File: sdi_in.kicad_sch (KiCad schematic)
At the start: 20 parts, among them J1 Conn_Coaxial, U1 LMH0344SQE_NOPB

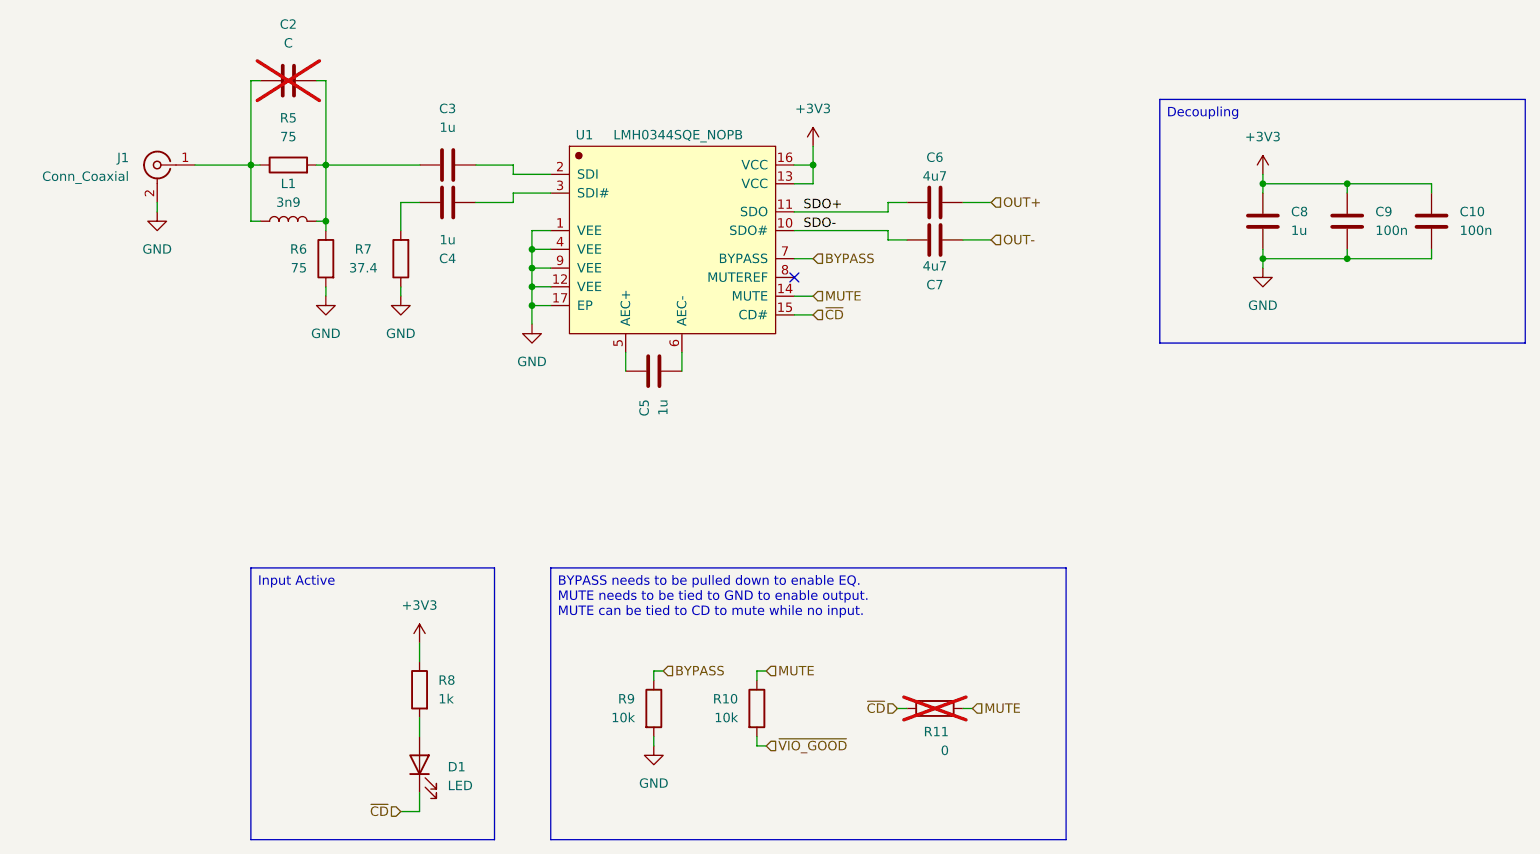
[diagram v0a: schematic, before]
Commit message: add power led and test points
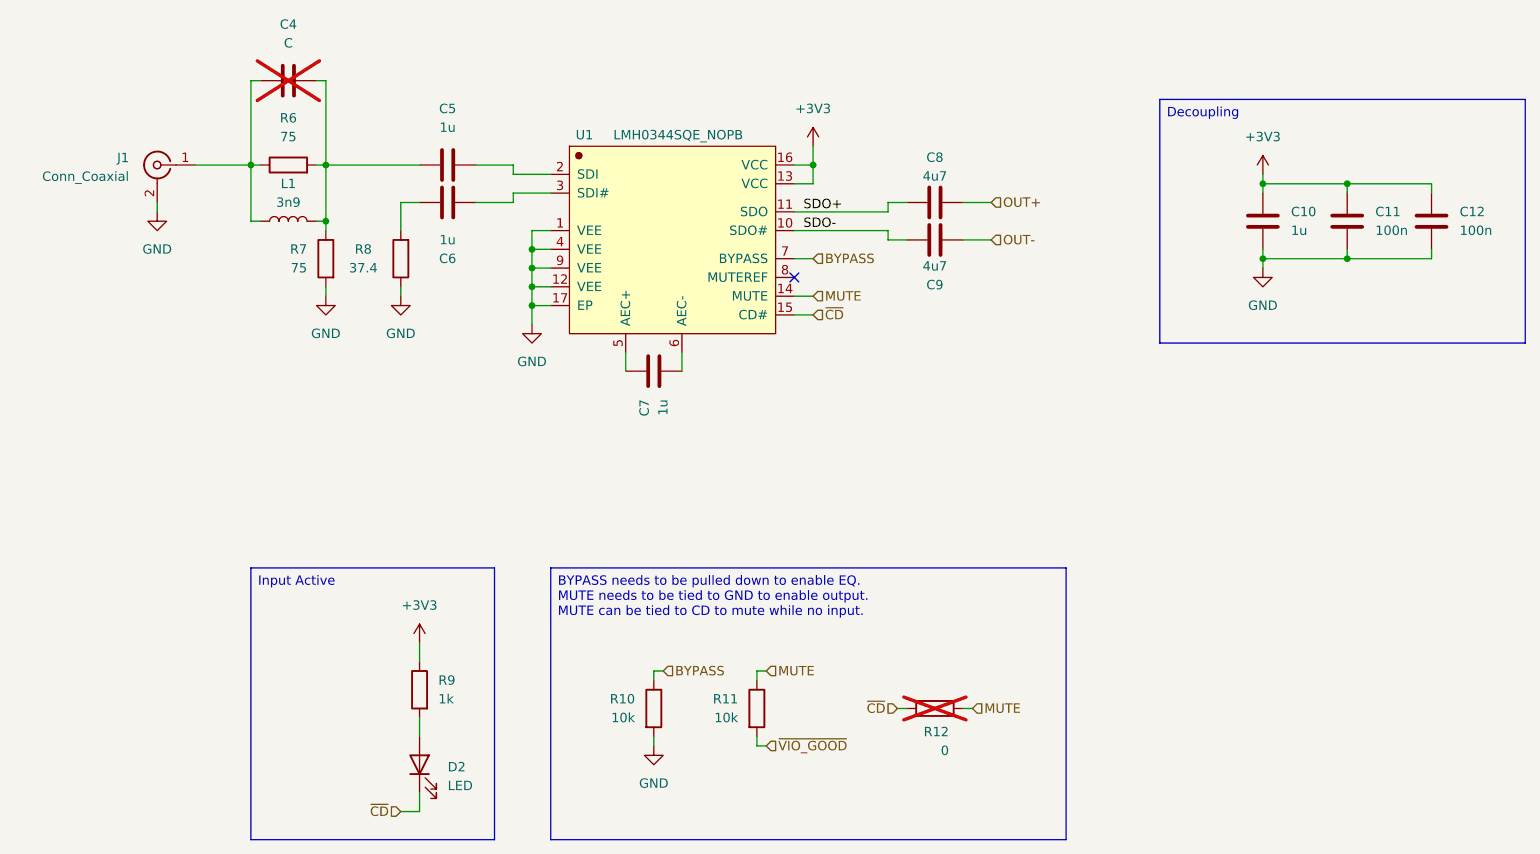
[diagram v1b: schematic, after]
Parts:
- renumbered C8 to C10, C9 to C11, C10 to C12, C2 to C4, C3 to C5, C4 to C6, C5 to C7, C6 to C8, C7 to C9, D1 to D2, R9 to R10, R10 to R11, R11 to R12, R5 to R6, R6 to R7, R7 to R8, R8 to R9

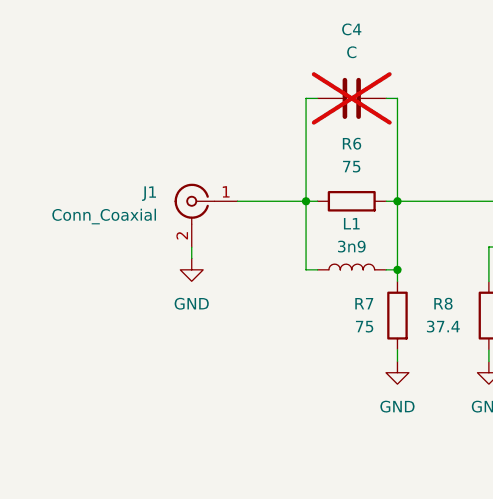
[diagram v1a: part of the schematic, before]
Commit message: check against jlcpcb capabilities
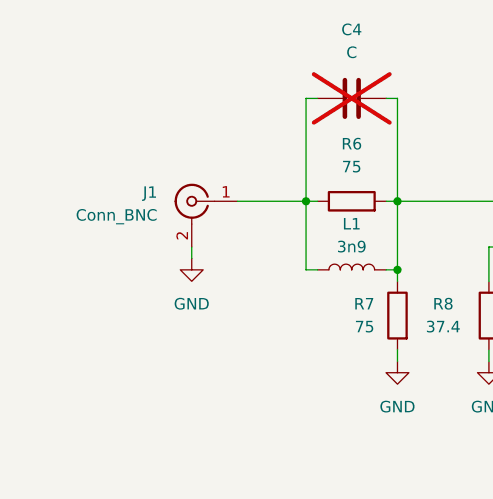
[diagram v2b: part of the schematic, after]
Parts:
- J1: value Conn_Coaxial -> Conn_BNC
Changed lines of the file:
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@@
 			)
 		)
-		(property "Value" "Conn_Coaxial"
+		(property "Value" "Conn_BNC"
 			(at 50.8 70.1431 0)
 			(show_name no)

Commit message: add some larger bypass caps to the cable drivers
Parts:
- renumbered C9 to C10, C10 to C11, C11 to C12, C12 to C13, C4 to C5, C5 to C6, C6 to C7, C7 to C8, C8 to C9

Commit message: specify skus for parts
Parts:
- C10, C9: LCSC (none) -> C69335
- C11, C8: LCSC (none) -> C6119818
- C12, C13: LCSC (none) -> C282519
- C6, C7: LCSC (none) -> C29266
- L1: LCSC (none) -> C412279
- R10, R11: LCSC (none) -> C25804
- R12: LCSC (none) -> C15402
- R6, R7: LCSC (none) -> C324774
- R8: LCSC (none) -> C2091522
- R9: LCSC (none) -> C21190
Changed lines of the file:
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@@
+			)
+		)
+		(property "LCSC" "C25804"
+			(at 121.92 142.24 0)
+			(hide yes)
+			(show_name no)
+			(do_not_autoplace no)
+			(effects
+				(font
+					(size 1.27 1.27)
+				)
 			)
 		)
@@
 			)
 		)
+		(property "LCSC" "C69335"
+			(at 160.02 73.66 90)
+			(hide yes)
+			(show_name no)
+			(do_not_autoplace no)
+			(effects
+				(font
+					(size 1.27 1.27)
+				)
+			)
+		)
 		(pin "2"
 		)
@@
 			)
 		)
+		(property "LCSC" "C29266"
+			(at 93.98 73.66 90)
+			(hide yes)
+			(show_name no)
+			(do_not_autoplace no)
+			(effects
+				(font
+					(size 1.27 1.27)
+				)
+			)
+		)
 		(pin "1"
 		)
@@
 		(property "KiLib_Generator" "SMD_2terminal_chip_molded"
 			(at 160.02 142.24 0)
+			(hide yes)
+			(show_name no)
+			(do_not_autoplace no)
+			(effects
+				(font
+					(size 1.27 1.27)
+				)
+			)
+		)
+		(property "LCSC" "C15402"
+			(at 160.02 142.24 90)
 			(hide yes)
 			(show_name no)
@@
 			)
 		)
+		(property "LCSC" "C412279"
+			(at 72.39 76.2 90)
+			(hide yes)
+			(show_name no)
+			(do_not_autoplace no)
+			(effects
+				(font
+					(size 1.27 1.27)
+				)
+			)
+		)
 		(pin "2"
 		)
@@
 			)
 		)
+		(property "LCSC" "C324774"
+			(at 72.39 68.58 90)
+			(hide yes)
+			(show_name no)
+			(do_not_autoplace no)
+			(effects
+				(font
+					(size 1.27 1.27)
+				)
+			)
+		)
 		(pin "2"
 		)
@@
 			)
 		)
+		(property "LCSC" "C69335"
+			(at 160.02 78.74 90)
+			(hide yes)
+			(show_name no)
+			(do_not_autoplace no)
+			(effects
+				(font
+					(size 1.27 1.27)
+				)
+			)
+		)
 		(pin "2"
 		)
@@
 		)
 		(property "KiLib_Generator" "SMD_2terminal_chip_molded"
+			(at 121.92 96.52 0)
+			(hide yes)
+			(show_name no)
+			(do_not_autoplace no)
+			(effects
+				(font
+					(size 1.27 1.27)
+				)
+			)
+		)
+		(property "LCSC" "C6119818"
 			(at 121.92 96.52 0)
 			(hide yes)
@@
 			)
 		)
+		(property "LCSC" "C29266"
+			(at 93.98 68.58 90)
+			(hide yes)
+			(show_name no)
+			(do_not_autoplace no)
+			(effects
+				(font
+					(size 1.27 1.27)
+				)
+			)
+		)
 		(pin "1"
 		)
@@
 		)
 		(property "KiLib_Generator" "SMD_2terminal_chip_molded"
+			(at 135.89 142.24 0)
+			(hide yes)
+			(show_name no)
+			(do_not_autoplace no)
+			(effects
+				(font
+					(size 1.27 1.27)
+				)
+			)
+		)
+		(property "LCSC" "C25804"
 			(at 135.89 142.24 0)
 			(hide yes)
@@
 			)
 		)
+		(property "LCSC" "C21190"
+			(at 90.17 139.7 0)
+			(hide yes)
+			(show_name no)
+			(do_not_autoplace no)
+			(effects
+				(font
+					(size 1.27 1.27)
+				)
+			)
+		)
 		(pin "1"
 		)
@@
 			)
 		)
+		(property "LCSC" "C6119818"
+			(at 204.47 76.2 0)
+			(hide yes)
+			(show_name no)
+			(do_not_autoplace no)
+			(effects
+				(font
+					(size 1.27 1.27)
+				)
+			)
+		)
 		(pin "2"
 		)
@@
 			)
 		)
+		(property "LCSC" "C282519"
+			(at 227.33 76.2 0)
+			(hide yes)
+			(show_name no)
+			(do_not_autoplace no)
+			(effects
+				(font
+					(size 1.27 1.27)
+				)
+			)
+		)
 		(pin "2"
 		)
@@
 			)
 		)
+		(property "LCSC" "C282519"
+			(at 215.9 76.2 0)
+			(hide yes)
+			(show_name no)
+			(do_not_autoplace no)
+			(effects
+				(font
+					(size 1.27 1.27)
+				)
+			)
+		)
 		(pin "2"
 		)
@@
 			)
 		)
+		(property "LCSC" "C2091522"
+			(at 87.63 81.28 0)
+			(hide yes)
+			(show_name no)
+			(do_not_autoplace no)
+			(effects
+				(font
+					(size 1.27 1.27)
+				)
+			)
+		)
 		(pin "2"
 		)
@@
 			(at 77.47 81.28 0)
 			(hide yes)
+			(show_name no)
+			(do_not_autoplace no)
+			(effects
+				(font
+					(size 1.27 1.27)
+				)
+			)
+		)
+		(property "LCSC" "C324774"
+			(at 77.47 81.28 0)
+			(hide yes)

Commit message: specify led colours
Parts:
- D2: value LED -> LED Green
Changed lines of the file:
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@@
 		(exclude_from_sim no)
 		(at 67.31 123.19 0)
-		(size 33.02 36.83)
+		(size 38.1 36.83)
 		(margins 0.9525 0.9525 0.9525 0.9525)
 		(stroke
@@
 			)
 		)
-		(property "Value" "LED"
+		(property "Value" "LED Green"
 			(at 93.98 152.7174 90)
 			(show_name no)

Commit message: sku and led resistor updates following review
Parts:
- C6, C7: LCSC C29266 -> C49210445
- D2: LCSC (none) -> C965804
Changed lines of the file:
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@@
 			)
 		)
-		(property "LCSC" "C29266"
+		(property "LCSC" "C49210445"
 			(at 93.98 73.66 90)
 			(hide yes)
@@
 			)
 		)
+		(property "LCSC" "C965804"
+			(at 90.17 149.86 90)
+			(hide yes)
+			(show_name no)
+			(do_not_autoplace no)
+			(effects
+				(font
+					(size 1.27 1.27)
+				)
+			)
+		)
 		(pin "1"
 		)
@@
 			)
 		)
-		(property "LCSC" "C29266"
+		(property "LCSC" "C49210445"
 			(at 93.98 68.58 90)
 			(hide yes)
